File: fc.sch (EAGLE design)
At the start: 48 parts, among them IC1 FT230XQ, IC2 BN055, U2 ATMEGA2560-16AU100A-M, Y1 16MHz, Y2 32.768kHz

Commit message: First draft of the schematic finished
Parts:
- removed R20, R21: 5.6, rcl:R-EU_R0603
- added LED0, LED5, LED6, LED7: (no value), led:LEDCHIP-LED0603
- added PPM0, PPM1, PPM2, PPM3, PPM4, PPM5, PPM6, PPM7, SBUS: (no value), pinhead:PINHD-1X3
- added R10, R11, R12: 100, rcl:R-EU_R0603
- added R2: (no value), resistor:R-EU_R0603
- added U$1: BSS138, hwp_SS18:BSS138
- R15, R16, R17: value 10k -> 100
- R18, R19: value 5.6 -> 100
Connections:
- removed net !ALERT_+3V3: R17.1, U2A.(T3/INT6)_PE6
- removed net !ALERT_+5V: R16.1, U2A.(OC3C/INT5)_PE5
- removed net !ALERT_VBAT: R15.1, U2A.(OC3B/INT4)_PE4
- removed net N$14: R21.2, U2A.(OC5A)_PL3
- removed net N$17: R20.2, U2A.(T5)_PL2
- removed net N$19: R18.2, U2A.(ICP4)_PL0
- removed net N$21: LED2.A, R19.1
- removed net N$23: LED4.A, R21.1
- new net !SBUS: R2.1, U$1.D, U2A.(RXD2)_PH0
- new net LED0: R15.2, U2A.(ICP4)_PL0
- new net LED1: R10.2, U2A.(ICP5)_PL1
- new net LED2: R11.2, U2A.(T5)_PL2
- new net LED3: R12.2, U2A.(OC5A)_PL3
- new net LED4: R16.2, U2A.(OC5B)_PL4
- new net LED5: R17.2, U2A.(OC5C)_PL5
- new net LED6: R18.2, U2A.PL6
- new net LED7: R19.2, U2A.PL7
- new net N$15: LED1.A, R10.1
- new net N$24: LED5.A, R17.1
- new net N$27: LED6.A, R18.1
- new net N$29: LED7.A, R19.1
- new net N$31: LED0.A, R15.1
- new net PPM0: PPM0.1, U2A.(OC1A/PCINT5)_PB5
- new net PPM1: PPM1.1, U2A.(OC1B/PCINT6)_PB6
- new net PPM2: PPM2.1, U2A.(OC0A/OC1C/PCINT7)_PB7
- new net PPM3: PPM3.1, U2A.(OC3A/AIN1)_PE3
- new net PPM4: PPM4.1, U2A.(OC3B/INT4)_PE4
- new net PPM5: PPM5.1, U2A.(OC3C/INT5)_PE5
- new net PPM6: PPM6.1, U2A.(OC4A)_PH3
- new net PPM7: PPM7.1, U2A.(OC4B)_PH4
- new net SBUS: SBUS.1, U$1.G
- net +3V3: now also R2.2; no longer R15.2, R16.2, R17.2
- net +5V: now also PPM0.2, PPM1.2, PPM2.2, PPM3.2, PPM4.2, PPM5.2, PPM6.2, PPM7.2, SBUS.2
- net GND: now also LED0.C, LED5.C, LED6.C, LED7.C, PPM0.3, PPM1.3, PPM2.3, PPM3.3, PPM4.3, PPM5.3, PPM6.3, PPM7.3, SBUS.3, U$1.S
- net N$18: now also LED2.A, R11.1; no longer R19.2, U2A.(ICP5)_PL1
- net N$20: now also LED3.A, R12.1; no longer LED1.A, R18.1
- net N$22: now also LED4.A, R16.1; no longer LED3.A, R20.1

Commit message: Initial draft for the layout
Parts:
- removed R13, R14: 10k, rcl:R-EU_R0603
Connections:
- removed net SCL: R13.1, U2A.(SCL/INT0)_PD0
- removed net SDA: R14.1, U2A.(SDA/INT1)_PD1
- net +3V3: now also C10.1, C11.1, C12.1, C15.1, C16.1, C17.1, C8.1, C9.1, IC1.3V3OUT, IC1.VCC, IC1.VCCIO, ISP.2, LED_RX.A, LED_TX.A, R3.2, U2B.AREF, U2B.AVCC, U2B.VCC, U2B.VCC_2, U2B.VCC_3, U2B.VCC_4; no longer R13.2, R14.2
- net +5V: no longer C10.1, C11.1, C12.1, C15.1, C16.1, C17.1, C8.1, C9.1, IC1.3V3OUT, IC1.VCC, IC1.VCCIO, ISP.2, LED_RX.A, LED_TX.A, R3.2, U2B.AREF, U2B.AVCC, U2B.VCC, U2B.VCC_2, U2B.VCC_3, U2B.VCC_4

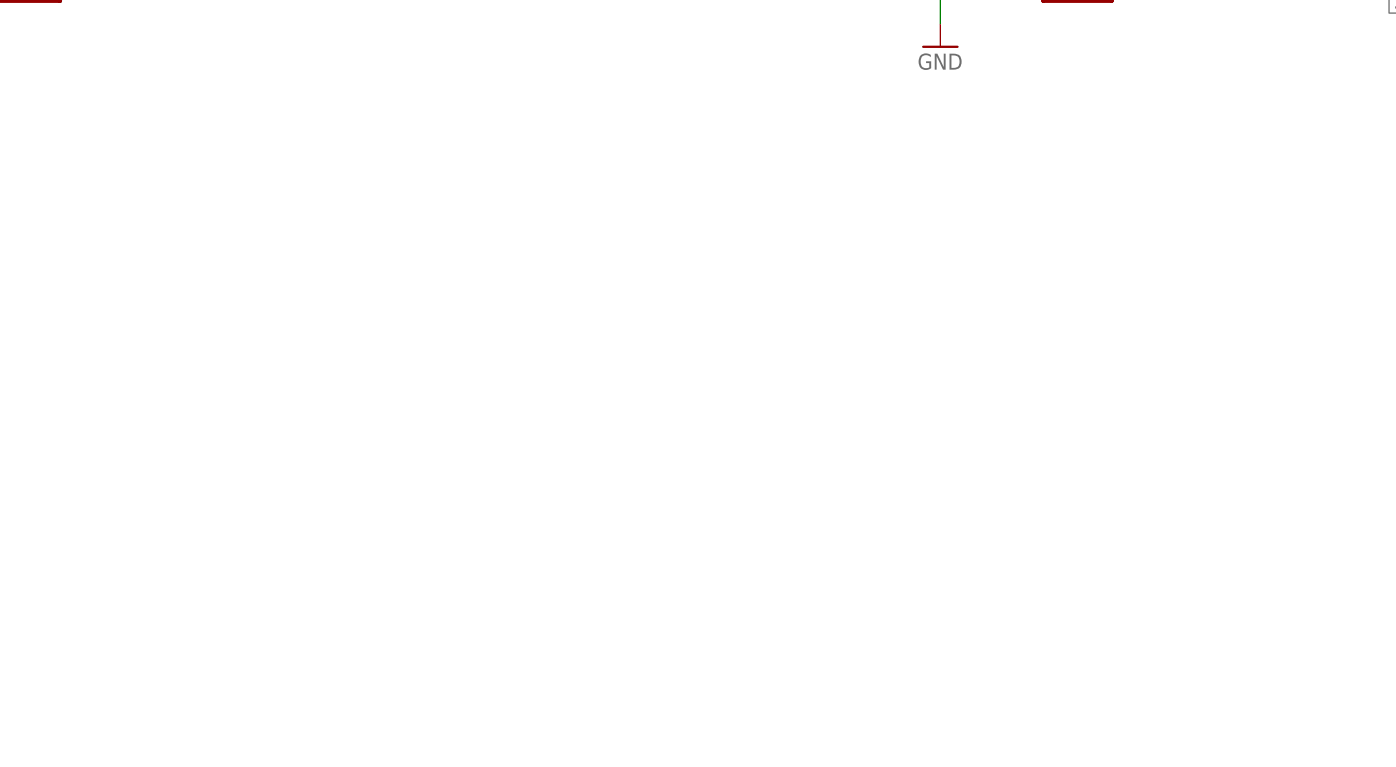
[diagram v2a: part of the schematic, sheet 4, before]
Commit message: Small changes, added reset button
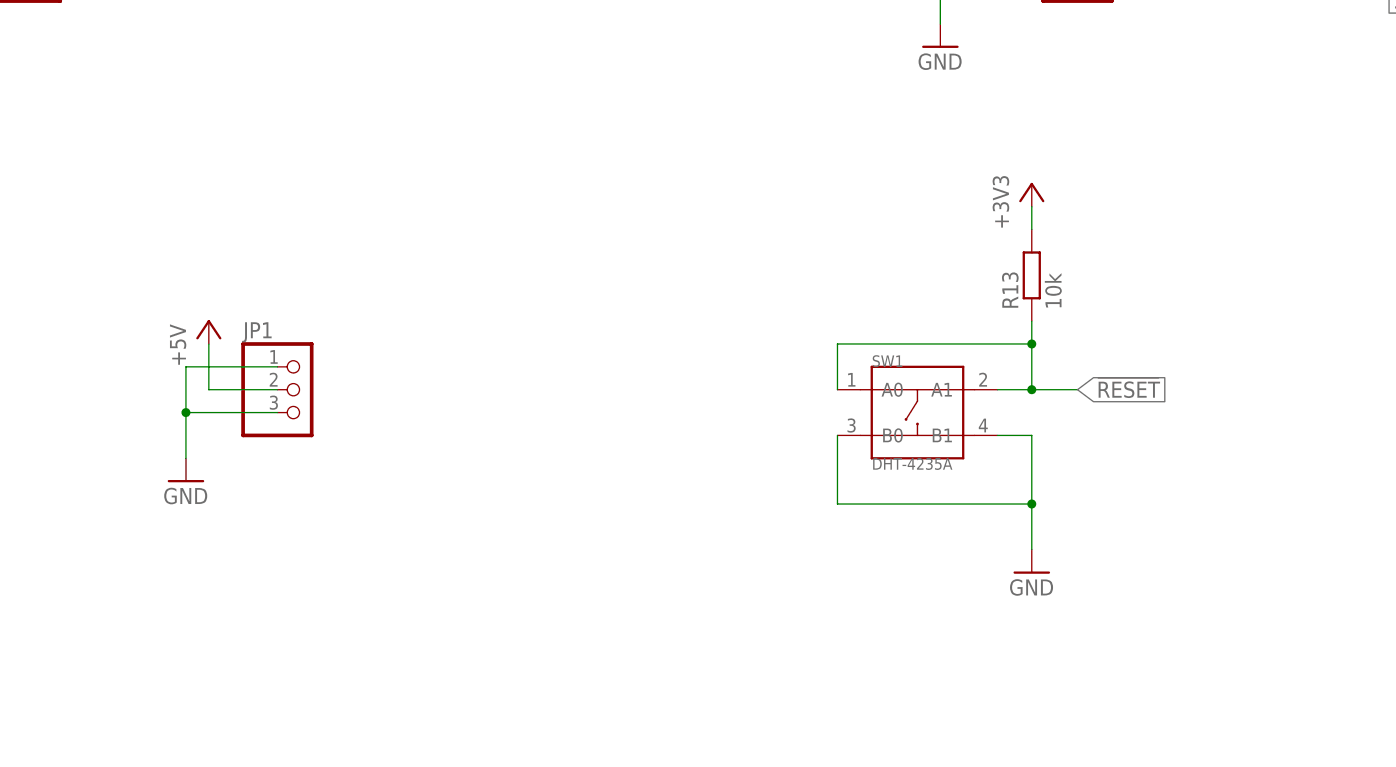
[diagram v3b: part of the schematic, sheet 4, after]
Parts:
- added JP1: (no value), pinhead:PINHD-1X3
- added R13: 10k, resistor:R-EU_R0603
- added SW1: DHT-4235A, Seeed-Switch:SMD-BUTTON-TOP-DHT-4235A(4P-4.2X3.2MM)
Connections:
- net !RESET: now also R13.1, SW1.A0, SW1.A1
- net +3V3: now also R13.2
- net +5V: now also JP1.2
- net GND: now also JP1.1, JP1.3, SW1.B0, SW1.B1
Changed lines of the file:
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@@
 <part name="+3V2" library="supply1" library_urn="urn:adsk.eagle:library:371" deviceset="+3V3" device=""/>
 <part name="GND8" library="supply1" library_urn="urn:adsk.eagle:library:371" deviceset="GND" device=""/>
-<part name="R1" library="resistor" library_urn="urn:adsk.eagle:library:348" deviceset="R-EU_" device="R0603" package3d_urn="urn:adsk.eagle:package:26057/1" value="10k"/>
+<part name="R1" library="resistor" library_urn="urn:adsk.eagle:library:348" deviceset="R-EU_" device="R0603" package3d_urn="urn:adsk.eagle:package:23555/2" value="10k"/>
 <part name="+3V3" library="supply1" library_urn="urn:adsk.eagle:library:371" deviceset="+3V3" device=""/>
 <part name="GND9" library="supply1" library_urn="urn:adsk.eagle:library:371" deviceset="GND" device=""/>
@@
 <part name="U$1" library="hwp_SS18" deviceset="BSS138" device=""/>
 <part name="+3V5" library="supply1" library_urn="urn:adsk.eagle:library:371" deviceset="+3V3" device=""/>
-<part name="R2" library="resistor" library_urn="urn:adsk.eagle:library:348" deviceset="R-EU_" device="R0603" package3d_urn="urn:adsk.eagle:package:26057/1"/>
+<part name="R2" library="resistor" library_urn="urn:adsk.eagle:library:348" deviceset="R-EU_" device="R0603" package3d_urn="urn:adsk.eagle:package:23555/2"/>
 <part name="GND15" library="supply1" library_urn="urn:adsk.eagle:library:371" deviceset="GND" device=""/>
 <part name="GND16" library="supply1" library_urn="urn:adsk.eagle:library:371" deviceset="GND" device=""/>
@@
 <part name="R19" library="rcl" library_urn="urn:adsk.eagle:library:334" deviceset="R-EU_" device="R0603" package3d_urn="urn:adsk.eagle:package:23555/2" value="100"/>
 <part name="LED7" library="led" library_urn="urn:adsk.eagle:library:259" deviceset="LED" device="CHIP-LED0603" package3d_urn="urn:adsk.eagle:package:15819/3"/>
+<part name="JP1" library="pinhead" library_urn="urn:adsk.eagle:library:325" deviceset="PINHD-1X3" device="" package3d_urn="urn:adsk.eagle:package:22458/2"/>
+<part name="P+8" library="supply1" library_urn="urn:adsk.eagle:library:371" deviceset="+5V" device=""/>
+<part name="GND7" library="supply1" library_urn="urn:adsk.eagle:library:371" deviceset="GND" device=""/>
+<part name="SW1" library="Seeed-Switch" library_urn="urn:adsk.eagle:library:476" deviceset="SMD-BUTTON-TOP-DHT-4235A(4P-4.2X3.2MM)" device="" package3d_urn="urn:adsk.eagle:package:32986/1" value="DHT-4235A"/>
+<part name="GND18" library="supply1" library_urn="urn:adsk.eagle:library:371" deviceset="GND" device=""/>
+<part name="+3V6" library="supply1" library_urn="urn:adsk.eagle:library:371" deviceset="+3V3" device=""/>
+<part name="R13" library="resistor" library_urn="urn:adsk.eagle:library:348" deviceset="R-EU_" device="R0603" package3d_urn="urn:adsk.eagle:package:23555/2" value="10k"/>
 </parts>
 <sheets>
@@
 <instance part="R19" gate="G$1" x="50.8" y="119.38" rot="R180"/>
 <instance part="LED7" gate="G$1" x="63.5" y="119.38" rot="R90"/>
+<instance part="JP1" gate="A" x="175.26" y="172.72"/>
+<instance part="P+8" gate="1" x="165.1" y="180.34"/>
+<instance part="GND7" gate="1" x="162.56" y="162.56"/>
+<instance part="SW1" gate="G$1" x="243.84" y="170.18"/>
+<instance part="GND18" gate="1" x="256.54" y="152.4"/>
+<instance part="+3V6" gate="G$1" x="256.54" y="195.58"/>
+<instance part="R13" gate="G$1" x="256.54" y="185.42" rot="R90"/>
 </instances>
 <busses>
@@
 <wire x1="246.38" y1="220.98" x2="246.38" y2="228.6" width="0.1524" layer="91"/>
 <pinref part="P+7" gate="1" pin="+5V"/>
+</segment>
+<segment>
+<pinref part="JP1" gate="A" pin="2"/>
+<wire x1="172.72" y1="172.72" x2="165.1" y2="172.72" width="0.1524" layer="91"/>
+<wire x1="165.1" y1="172.72" x2="165.1" y2="177.8" width="0.1524" layer="91"/>
+<pinref part="P+8" gate="1" pin="+5V"/>
 </segment>
 </net>
@@
 <pinref part="GND17" gate="1" pin="GND"/>
 </segment>
+<segment>
+<pinref part="JP1" gate="A" pin="1"/>
+<wire x1="172.72" y1="175.26" x2="162.56" y2="175.26" width="0.1524" layer="91"/>
+<pinref part="JP1" gate="A" pin="3"/>
+<wire x1="172.72" y1="170.18" x2="162.56" y2="170.18" width="0.1524" layer="91"/>
+<wire x1="162.56" y1="170.18" x2="162.56" y2="175.26" width="0.1524" layer="91"/>
+<wire x1="162.56" y1="170.18" x2="162.56" y2="165.1" width="0.1524" layer="91"/>
+<junction x="162.56" y="170.18"/>
+<pinref part="GND7" gate="1" pin="GND"/>
+</segment>
+<segment>
+<pinref part="SW1" gate="G$1" pin="B1"/>
+<wire x1="252.73" y1="167.64" x2="256.54" y2="167.64" width="0.1524" layer="91"/>
+<wire x1="256.54" y1="167.64" x2="256.54" y2="160.02" width="0.1524" layer="91"/>
+<pinref part="SW1" gate="G$1" pin="B0"/>
+<wire x1="256.54" y1="160.02" x2="256.54" y2="154.94" width="0.1524" layer="91"/>
+<wire x1="256.54" y1="160.02" x2="234.95" y2="160.02" width="0.1524" layer="91"/>
+<wire x1="234.95" y1="160.02" x2="234.95" y2="167.64" width="0.1524" layer="91"/>
+<junction x="256.54" y="160.02"/>
+<pinref part="GND18" gate="1" pin="GND"/>
+</segment>
 </net>
 <net name="SBUS" class="0">
@@
 <wire x1="320.04" y1="238.76" x2="320.04" y2="241.3" width="0.1524" layer="91"/>
 </segment>
+<segment>
+<pinref part="R13" gate="G$1" pin="2"/>
+<pinref part="+3V6" gate="G$1" pin="+3V3"/>
+<wire x1="256.54" y1="190.5" x2="256.54" y2="193.04" width="0.1524" layer="91"/>
+</segment>
 </net>
 <net name="N$31" class="0">
@@
 </segment>
 </net>
+<net name="!RESET" class="0">
+<segment>
+<pinref part="SW1" gate="G$1" pin="A1"/>
+<wire x1="252.73" y1="172.72" x2="256.54" y2="172.72" width="0.1524" layer="91"/>
+<pinref part="SW1" gate="G$1" pin="A0"/>
+<wire x1="256.54" y1="172.72" x2="261.62" y2="172.72" width="0.1524" layer="91"/>
+<wire x1="234.95" y1="172.72" x2="234.95" y2="177.8" width="0.1524" layer="91"/>
+<wire x1="234.95" y1="177.8" x2="256.54" y2="177.8" width="0.1524" layer="91"/>
+<wire x1="256.54" y1="177.8" x2="256.54" y2="172.72" width="0.1524" layer="91"/>
+<junction x="256.54" y="172.72"/>
+<pinref part="R13" gate="G$1" pin="1"/>
+<wire x1="256.54" y1="177.8" x2="256.54" y2="180.34" width="0.1524" layer="91"/>
+<junction x="256.54" y="177.8"/>
+<label x="261.62" y="172.72" size="1.778" layer="95" xref="yes"/>
+</segment>
+</net>

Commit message: Improved the design
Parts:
- removed C13, C14: 47pF, rcl:C-EUC0603
- removed C6, C7: 8pF, rcl:C-EUC0603
- removed C8, C9: 100nF, rcl:C-EUC0603
- removed IC1: FT230XQ, ftdichip:FT230XQ
- removed ISP: (no value), pinhead:PINHD-2X3
- removed J3: (no value), adafruit:USBMINIB
- removed LED_RX, LED_TX: (no value), led:LEDCHIP-LED0603
- removed R13: 10k, resistor:R-EU_R0603
- removed R3: 10k, rcl:R-EU_R0603
- removed R4, R5: 5.6, rcl:R-EU_R0603
- removed R6, R7: 27, rcl:R-EU_R0603
- removed R8: 4k7, rcl:R-EU_R0603
- removed SW1: DHT-4235A, Seeed-Switch:SMD-BUTTON-TOP-DHT-4235A(4P-4.2X3.2MM)
- removed U2: ATMEGA2560-16AU100A-M, ATMEGA2560:ATMEGA2560-16AU100A-M
- removed Y1: 16MHz, SparkFun-Clocks:CRYSTALSMD-5X3.2-2PAD
- added C19, C20: 8pF, rcl:C-EUC0603
- added C21, C22, C23, C24, C25: 100nF, rcl:C-EUC0603
- added ISP1: (no value), pinhead:PINHD-2X3
- added J2: USBC, USBC:USBC
- added LED_RX1, LED_TX1: (no value), led:LEDCHIP-LED0603
- added R14: 270, rcl:R-EU_R0603
- added R20, R21: 27, rcl:R-EU_R0603
- added R22, R23: 4k7, rcl:R-EU_R0603
- added R35: 10k, resistor:R-EU_R0603
- added S2: FSMSM, switch:FSMSM
- added U1: ATMEGA2560-16AU100A-M, ATMEGA2560:ATMEGA2560-16AU100A-M
- added U4: FT230XQ, ftdichip:FT230XQ
- added U5: SI8621AB-B-IS, SI8621AB-B-IS:SI8621AB-B-IS
- added Y3: 16MHz, SparkFun-Clocks:CRYSTALSMD-5X3.2-2PAD
- C10, C11: value 100nF -> 47pF
- C12: value 100nF -> 10nF
- C17: device rcl:C-EUC0603 -> Kondensatoren (rev17a):WCAP-ASLI_4X5,5_865080640004
- R9: value 10k -> 270
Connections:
- removed net N$10: J3.D+, R6.2
- removed net N$11: J3.D-, R7.1
- removed net N$16: J3.VBUS, R8.2
- removed net N$6: IC1.CBUS2, R4.1
- removed net N$7: IC1.CBUS1, R5.1
- removed net N$8: LED_TX.C, R4.2
- removed net N$9: LED_RX.C, R5.2
- removed net VBUS_SENSE: IC1.CBUS0, R8.1, R9.2
- new net D+1: J2.DP1, J2.DP2, R20.2
- new net D-1: J2.DN1, J2.DN2, R21.1
- new net GNDIO: C10.1, C11.1, C12.2, C15.2, C16.2, C17.2, J2.GND, U4.GND, U4.GND@1, U5.GND1
- new net N$32: C19.2, U1A.XTAL1, Y3.2
- new net N$33: C20.2, U1A.XTAL2, Y3.1
- new net RXD: R23.1, U4.RXD, U5.A2
- new net TXD: R22.1, U4.TXD, U5.A1
- new net USBDM1: C11.2, R21.2, U4.USBDM
- new net USBDP1: C10.2, R20.1, U4.USBDP
- new net VBUS: C12.1, C16.1, C17.1, J2.VBUS, U4.VCC
- new net VCCIO: C15.1, LED_RX1.A, LED_TX1.A, R22.2, R23.2, U4.!RTS, U4.3V3OUT, U4.VCCIO, U5.VDD1
- net !BNO_RST: now also U1A.(ICP1)_PD4; no longer U2A.(XCK1)_PD5
- net !RESET: now also ISP1.5, R35.1, S2.2, U1A.!RESET; no longer ISP.5, R13.1, R3.1, SW1.A0, SW1.A1, U2A.!RESET
- net !SBUS: now also U1A.(RXD2)_PH0; no longer U2A.(RXD2)_PH0
- net +3V3: now also C21.1, C22.1, C23.1, C24.1, C25.1, ISP1.2, R35.2, U1B.AREF, U1B.AVCC, U1B.VCC, U1B.VCC_2, U1B.VCC_3, U1B.VCC_4, U5.VDD2; no longer C10.1, C11.1, C12.1, C15.1, C16.1, C17.1, C8.1, C9.1, IC1.3V3OUT, IC1.VCC, IC1.VCCIO, ISP.2, LED_RX.A, LED_TX.A, R13.2, R3.2, U2B.AREF, U2B.AVCC, U2B.VCC, U2B.VCC_2, U2B.VCC_3, U2B.VCC_4
- net BNO_INT: now also U1A.(OC2A/PCINT4)_PB4; no longer U2A.(ICP1)_PD4
- net BNO_RX: now also U1A.(TXD1/INT3)_PD3; no longer U2A.(TXD1/INT3)_PD3
- net BNO_TX: now also U1A.(RXD1/INT2)_PD2; no longer U2A.(RXD1/INT2)_PD2
- net GND: now also C19.1, C20.1, C21.2, C22.2, C23.2, C24.2, C25.2, ISP1.6, S2.1, U1B.GND, U1B.GND_2, U1B.GND_3, U1B.GND_4, U1B.GND_5, U5.GND2; no longer C10.2, C11.2, C12.2, C13.1, C14.1, C15.2, C16.2, C17.2, C6.1, C7.1, C8.2, C9.2, IC1.GND, IC1.GND@1, ISP.6, J3.GND, R9.1, SW1.B0, SW1.B1, U2B.GND, U2B.GND_2, U2B.GND_3, U2B.GND_4, U2B.GND_5
- net LED0: now also U1A.(ICP4)_PL0; no longer U2A.(ICP4)_PL0
- net LED1: now also U1A.(ICP5)_PL1; no longer U2A.(ICP5)_PL1
- net LED2: now also U1A.(T5)_PL2; no longer U2A.(T5)_PL2
- net LED3: now also U1A.(OC5A)_PL3; no longer U2A.(OC5A)_PL3
- net LED4: now also U1A.(OC5B)_PL4; no longer U2A.(OC5B)_PL4
- net LED5: now also U1A.(OC5C)_PL5; no longer U2A.(OC5C)_PL5
- net LED6: now also U1A.PL6; no longer U2A.PL6
- net LED7: now also U1A.PL7; no longer U2A.PL7
- net MISO: now also ISP1.1, U1A.(MISO/PCINT3)_PB3; no longer ISP.1, U2A.(MISO/PCINT3)_PB3
- net MOSI: now also ISP1.4, U1A.MOSI/PCINT2)_PB2; no longer ISP.4, U2A.MOSI/PCINT2)_PB2
- net N$2: now also R14.1, U4.CBUS1; no longer C6.2, U2A.XTAL1, Y1.2
- net N$3: now also LED_RX1.C, R9.2; no longer C7.2, U2A.XTAL2, Y1.1
- net N$4: now also LED_TX1.C, R14.2; no longer C13.2, IC1.USBDP, R6.1
- net N$5: now also R9.1, U4.CBUS2; no longer C14.2, IC1.USBDM, R7.2
- net PPM0: now also U1A.(OC1A/PCINT5)_PB5; no longer U2A.(OC1A/PCINT5)_PB5
- net PPM1: now also U1A.(OC1B/PCINT6)_PB6; no longer U2A.(OC1B/PCINT6)_PB6
- net PPM2: now also U1A.(OC0A/OC1C/PCINT7)_PB7; no longer U2A.(OC0A/OC1C/PCINT7)_PB7
- net PPM3: now also U1A.(OC3A/AIN1)_PE3; no longer U2A.(OC3A/AIN1)_PE3
- net PPM4: now also U1A.(OC3B/INT4)_PE4; no longer U2A.(OC3B/INT4)_PE4
- net PPM5: now also U1A.(OC3C/INT5)_PE5; no longer U2A.(OC3C/INT5)_PE5
- net PPM6: now also U1A.(OC4A)_PH3; no longer U2A.(OC4A)_PH3
- net PPM7: now also U1A.(OC4B)_PH4; no longer U2A.(OC4B)_PH4
- net SCK: now also ISP1.3, U1A.(SCK/PCINT1)_PB1; no longer ISP.3, U2A.(SCK/PCINT1)_PB1
- net USB_RX: now also U1A.(RXD0/PCINT8)_PE0, U5.B1; no longer IC1.TXD, U2A.(RXD0/PCINT8)_PE0
- net USB_TX: now also U1A.(TXD0)_PE1, U5.B2; no longer IC1.RXD, U2A.(TXD0)_PE1
